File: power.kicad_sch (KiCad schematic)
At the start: 78 parts, among them IC1 STM32MP157AAB3, IC3 STC3117IJT, IC4 MCP73830T-2AAI_MYY, IC5 MT41K256M16TW-107_P, IC6 STPMIC1BPQR, IC8 STUSB1600AQTR, J1 Conn_01x04, P1 USB_C_Plug_USB2.0

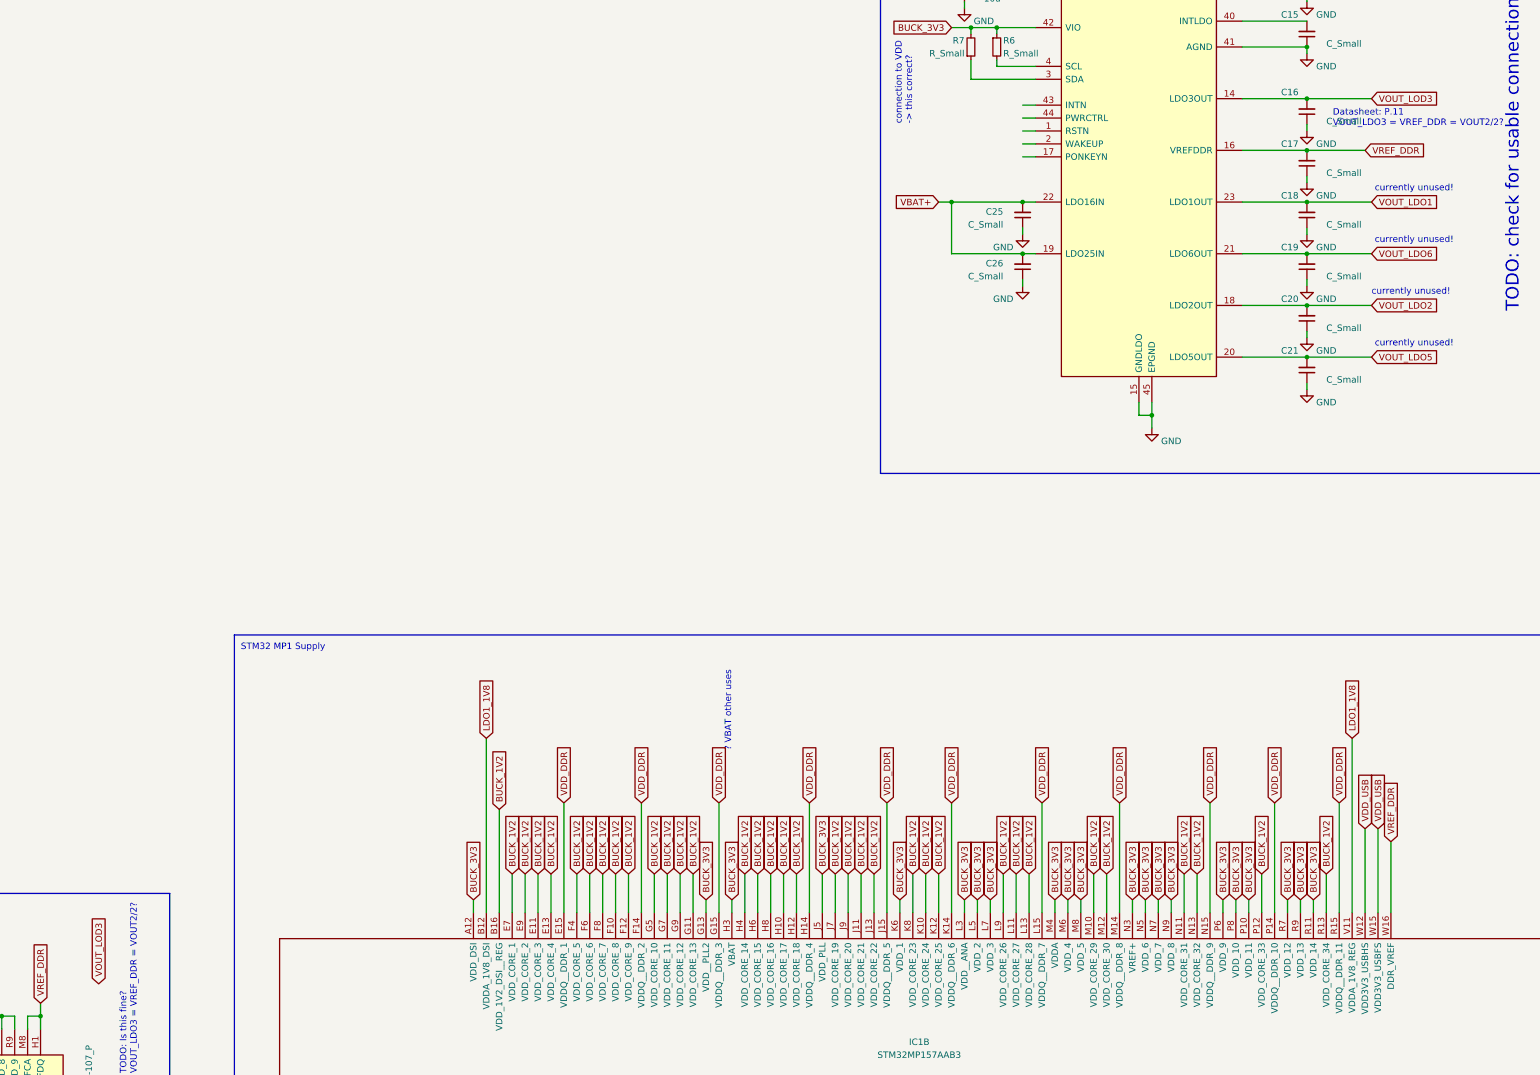
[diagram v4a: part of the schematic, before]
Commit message: Add DDR routing to STM32MP1
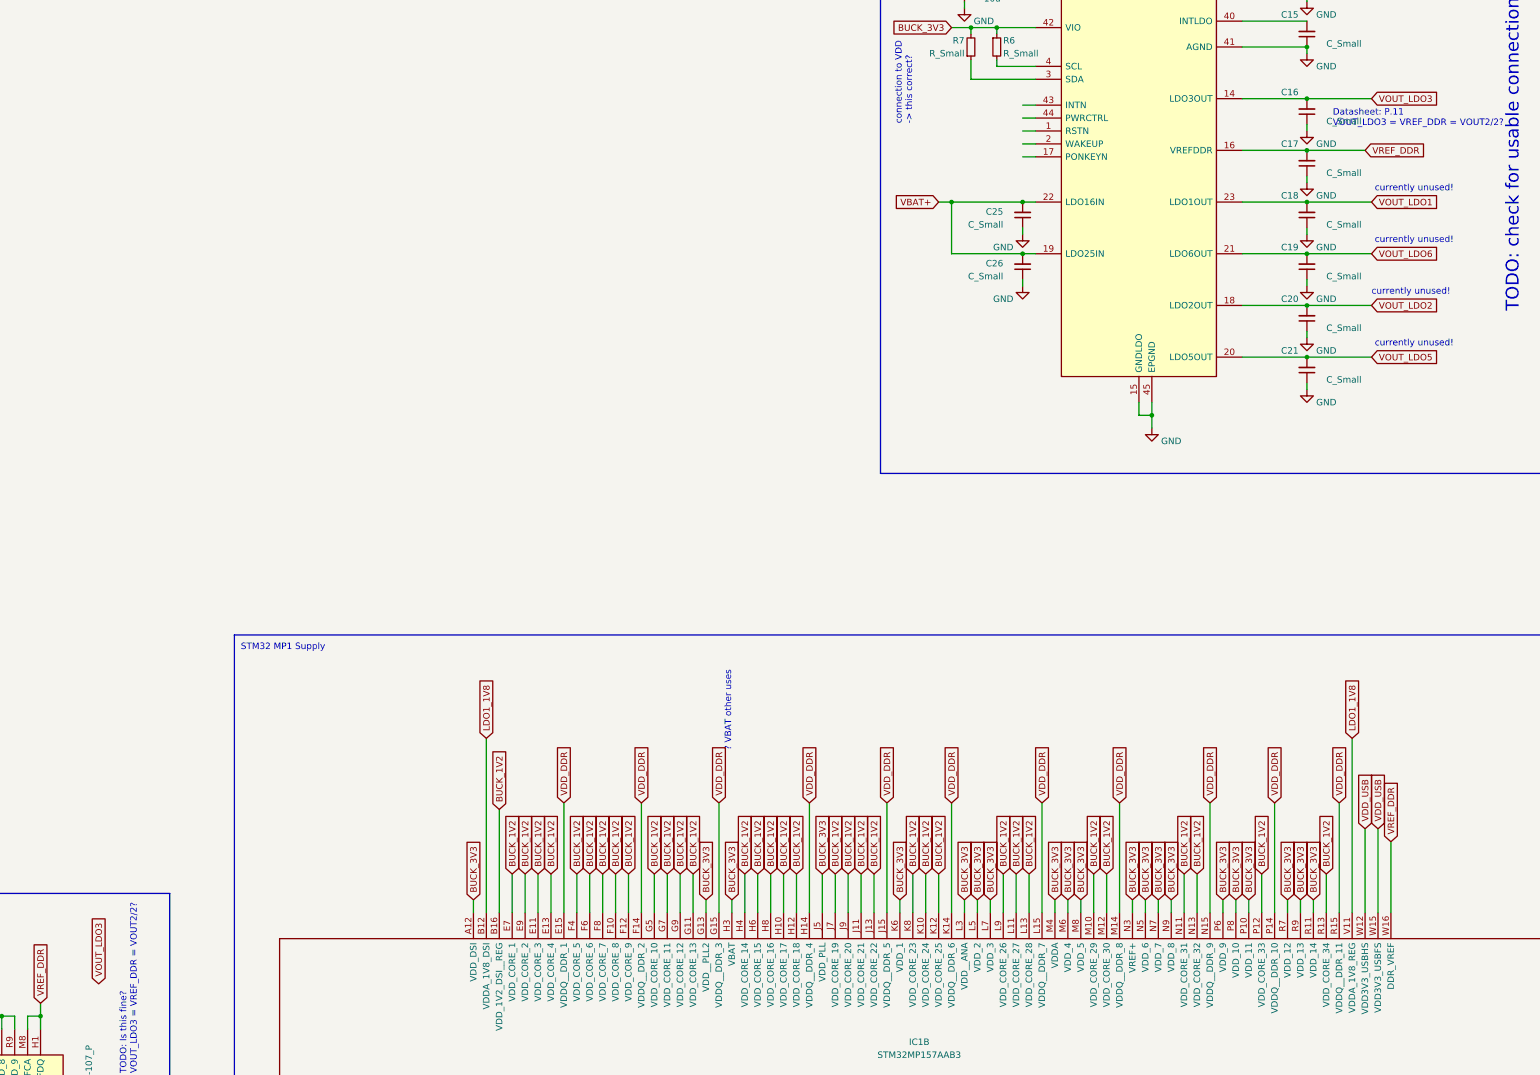
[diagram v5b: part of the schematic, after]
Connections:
- net VOUT_LOD3 renamed VOUT_LDO3
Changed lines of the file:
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@@
     )
   )
-  (global_label "VOUT_LOD3" (shape input) (at 515.62 135.89 0) (fields_autoplaced)
+  (global_label "VOUT_LDO3" (shape input) (at 515.62 135.89 0) (fields_autoplaced)
     (effects (font (size 1.27 1.27)) (justify left))
     (property "Intersheetrefs" "${INTERSHEET_REFS}" (at 529.0487 135.89 0)
@@
     )
   )
-  (global_label "VOUT_LOD3" (shape input) (at 265.43 309.88 90) (fields_autoplaced)
+  (global_label "VOUT_LDO3" (shape input) (at 265.43 309.88 90) (fields_autoplaced)
     (effects (font (size 1.27 1.27)) (justify left))
     (property "Intersheetrefs" "${INTERSHEET_REFS}" (at 265.43 296.4513 90)

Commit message: Added Q1 totem-pole circuit for STUSB. Moved components for better visibility.
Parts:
- added Q1: PMDPB70XP_115, ARMband:PMDPB70XP115, symbol ARMband:PMDPB70XP_115
- added R62: 0R, Resistor_SMD:R_0603_1608Metric, symbol Device:R_Small
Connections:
- net VIN: now also Q1.6 (D1_1), Q1.7 (D1_2), R62.1; no longer C31.2, D1.2 (A), IC4.4 (VDD)
- net at R16.1: now also IC8.24 (VDD), Q1.1 (S1), Q1.4 (S2)
- net at R16.2, R17.1: now also Q1.2 (G1), Q1.5 (G2)
- new net VIN_BAT_CHRG: C31.2, D1.2 (A), IC4.4 (VDD), Q1.3 (D2_1), Q1.8 (D2_2), R62.2
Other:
- note added: "Caution: Datasheet P. 123 "Each power supply pair (VDD /VSS , VDDCORE/VSS, VDDA/VSSA ...) must be decoupled with filtering ceramic capacitors. These capacitors must be placed as close as possible to, or below, the appropriate pins on the underside of the PCB to ensure good operation of the device.""
- note added: "Couloumb counter config in REG_CC_CNF: CC_CNF = (Rsens(mOhm) * Cnom_bat(mAh))/49.556 REG_CC_CNF is 395 by default (POR)"
- note added: "TODO"
- note added: "TODO: change to 1V8 use BUCK4, since it can supply 2A"
- note added: "To bat charger"
- note added: "VBAT other uses: Seems like this pin is used if you want to power it throug a battery. However, we already power our whole circuit through a battery + regulators. So connect regulators should be perfectly fine."
- note added: "VREF- == VSSA (== VSS?) Otherwise all GNDs can be linked together"
- note removed: "? VBAT other uses"
- note removed: "TODO: Is this fine? VOUT_LDO3 = VREF_DDR = VOUT2/2?"
- note removed: "TODO: all GND connections together?"
- note removed: "TODO: dual PMOS"
- note removed: "connection to VDD -> this correct?"
- moved on the sheet: BT1, C10, C11, C12, C13, C14, C15, C16, C17, C18, C19, C20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

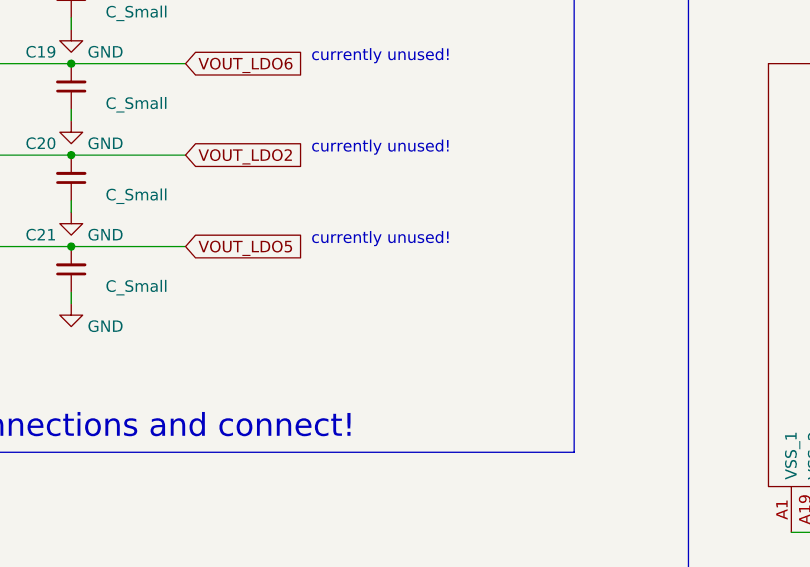
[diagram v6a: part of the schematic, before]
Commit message: Add level shifter for uSD
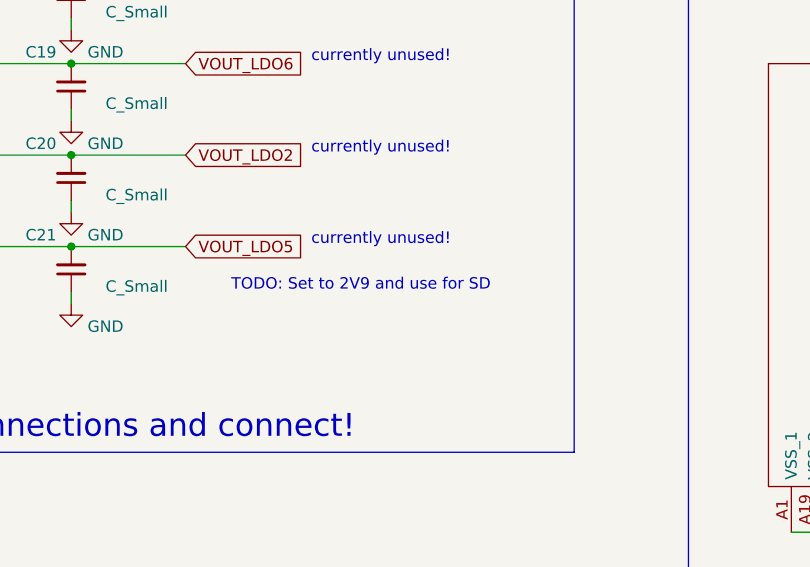
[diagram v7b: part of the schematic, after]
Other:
- note added: "TODO: Set to 2V9 and use for SD"
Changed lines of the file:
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@@
+    (effects (font (size 1.27 1.27)) (justify left bottom))
+  )
+  (text "TODO: Set to 2V9 and use for SD" (at 127 344.17 0)
     (effects (font (size 1.27 1.27)) (justify left bottom))
   )

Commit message: 3v3 to 1V8 rework
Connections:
- net BUCK_1V2 renamed BUCK1_1V2
- net BUCK_1V8 renamed BUCK3_3V3
- net BUCK3_3V3: now also C35.2, IC8.22 (VSYS)
- net BUCK_3V3 renamed BUCK4_1V8
- net BUCK4_1V8: no longer C35.2, IC8.22 (VSYS)
- net VDD_DDR renamed BUCK2_1V35
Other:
- note added: "3V3 2000mA @ HP mode 50 - 200mA @ LP mode VDDBUCK4_1V8_USBHS VDDBUCK4_1V8_USBFS"
- note added: "VSYS: power from system, connect to GND if not used Must be 3V-5V"
- note added: "connect to BUCK2_1V35 power plane"
- note added: "used for STUSB VSYS (3V-5V)"
- note removed: "3V3 2000mA @ HP mode 50 - 200mA @ LP mode VDDBUCK_3V3_USBHS VDDBUCK_3V3_USBFS"
- note removed: "VSYS: power from system, connect to GND if not used"
- note removed: "connect to VDD_DDR power plane"
- moved on the sheet: C10, C11, C12, C13, C14, C15, C16, C17, C18, C19, C20, C21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
